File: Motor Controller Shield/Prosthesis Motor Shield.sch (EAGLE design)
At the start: 46 parts, among them M1_ACT M02POLAR_LOCK, M2_ACT M02POLAR_LOCK, U1 74VHC14MTCX, U2 74VHC14MTCX

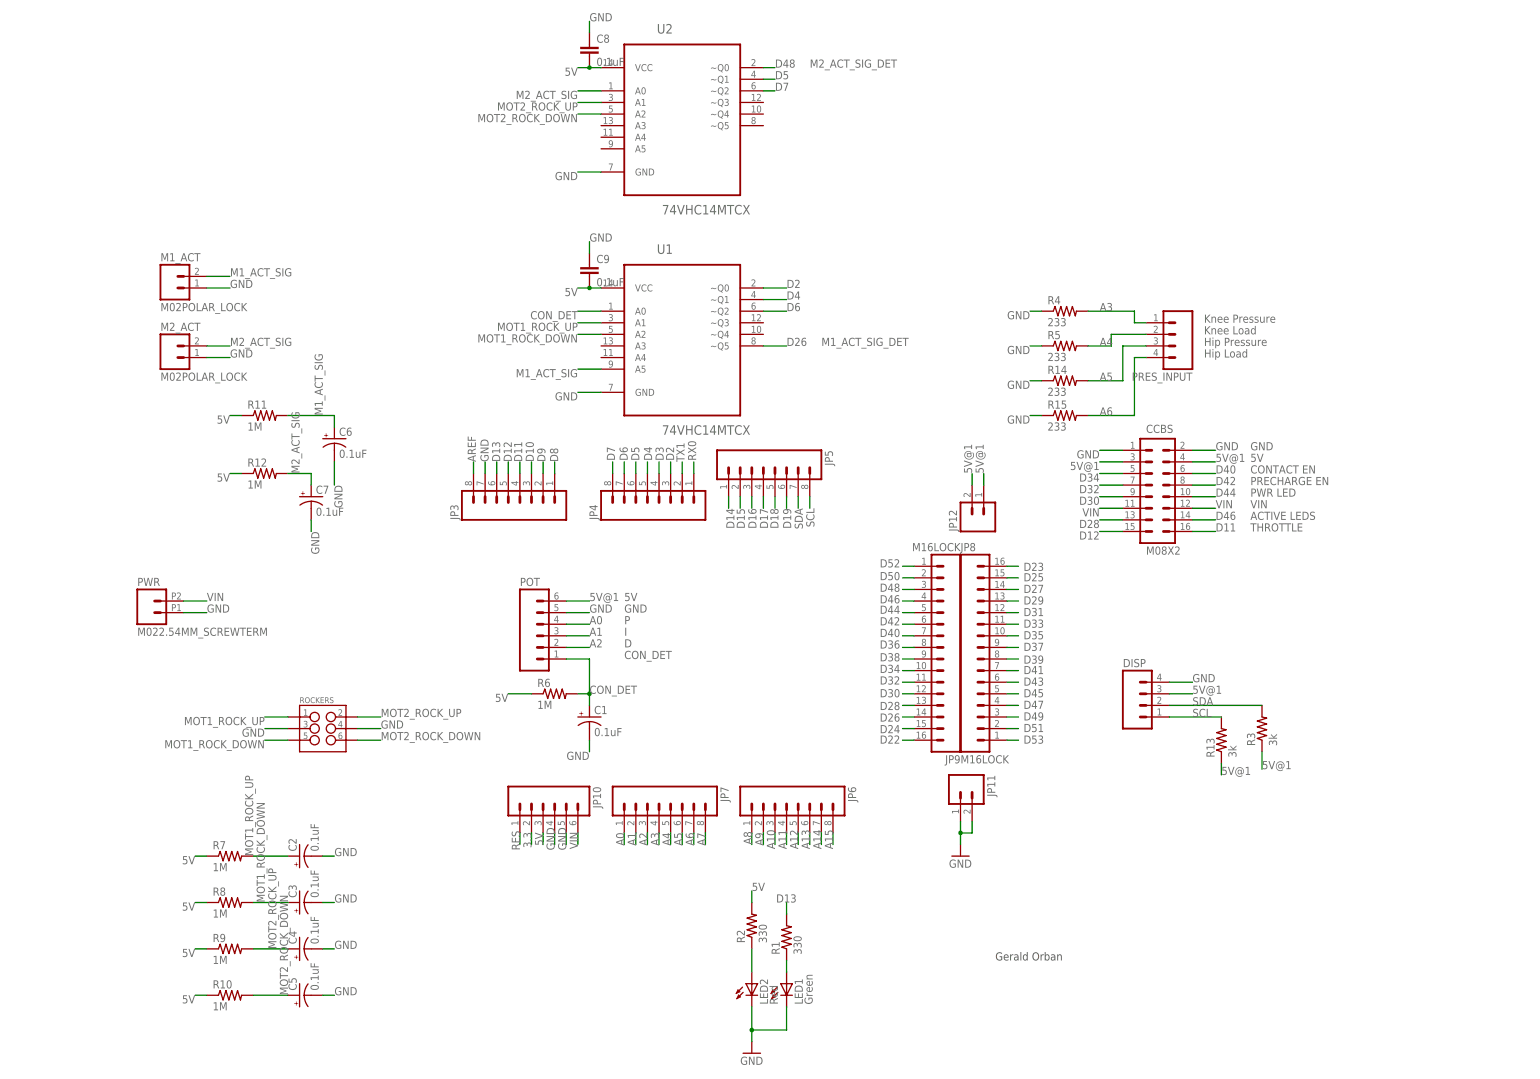
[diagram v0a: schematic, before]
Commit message: CHanged all connectors on MCB to use Molex
Changed most of the connectors on the BMS interface to use molex as
well.
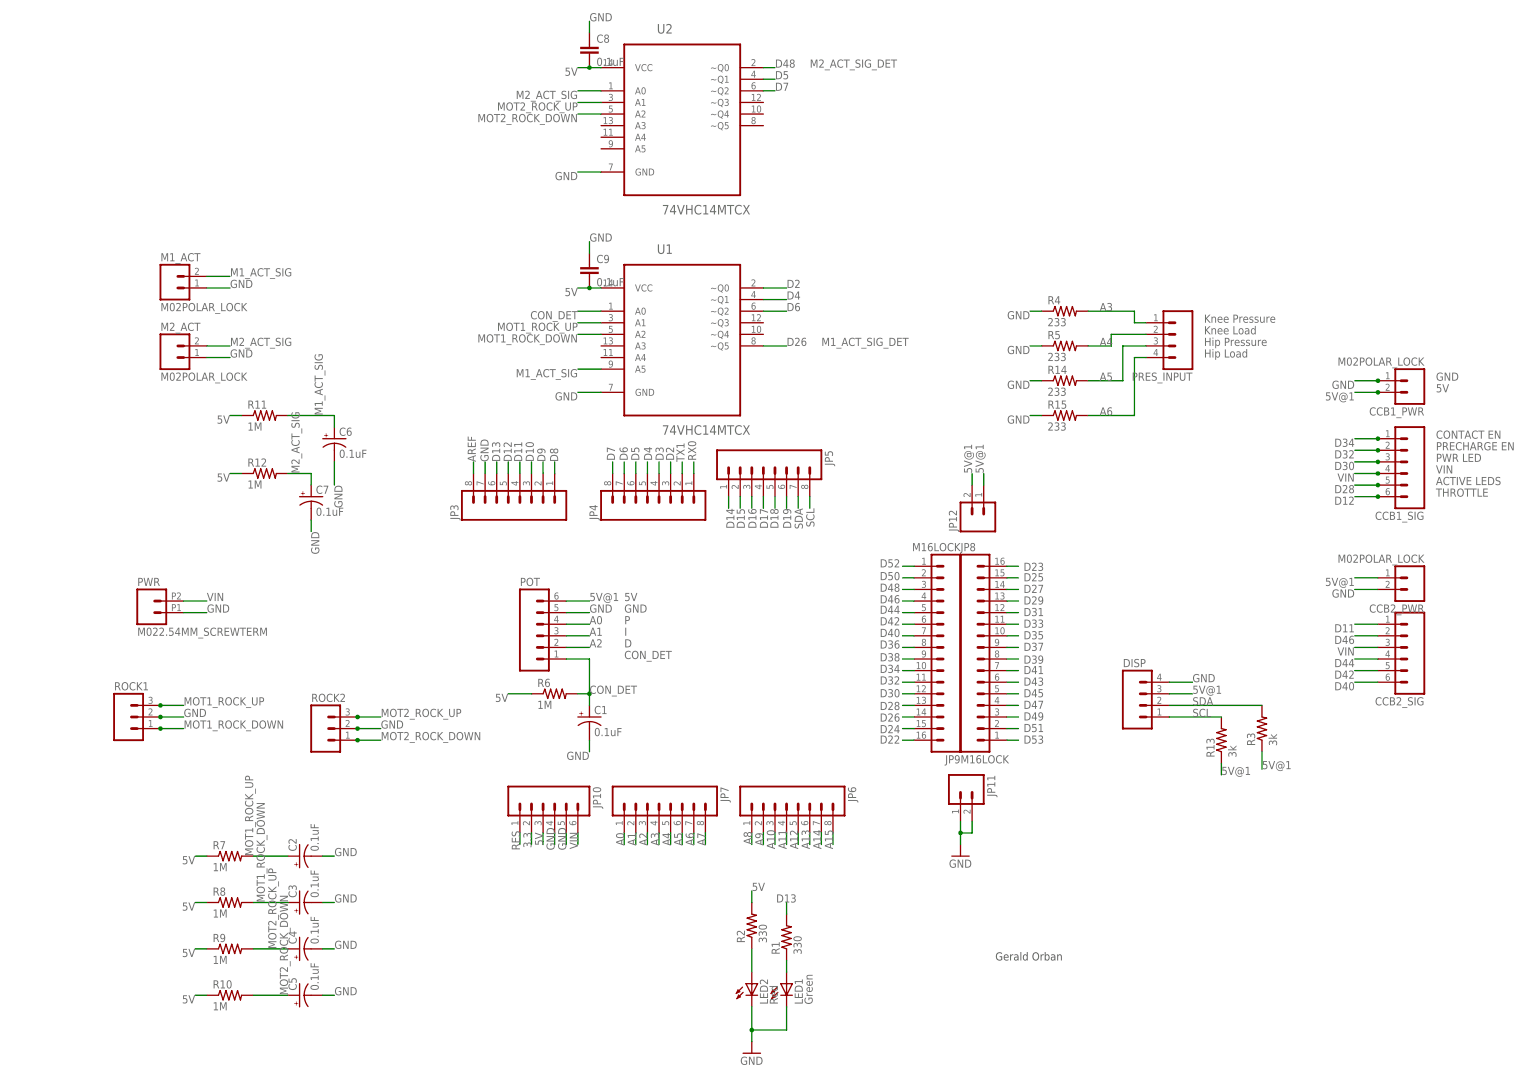
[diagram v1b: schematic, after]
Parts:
- removed CCBS: M08X2, SparkFun-Connectors:M08X2
- removed ROCKERS: (no value), SparkFun-Connectors:M03X2
- added CCB1_PWR, CCB2_PWR: M02POLAR_LOCK, SparkFun-Connectors:M02POLAR_LOCK
- added CCB1_SIG, CCB2_SIG: (no value), SparkFun-Connectors:M06POLAR_LOCK
- added ROCK1, ROCK2: (no value), SparkFun-Connectors:M03POLAR_LOCK
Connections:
- net 5V@1: now also CCB1_PWR.2, CCB2_PWR.1; no longer CCBS.3, CCBS.4
- net D11: now also CCB2_SIG.1; no longer CCBS.16
- net D12: now also CCB1_SIG.6; no longer CCBS.15
- net D28: now also CCB1_SIG.5; no longer CCBS.13
- net D30: now also CCB1_SIG.3; no longer CCBS.9
- net D32: now also CCB1_SIG.2; no longer CCBS.7
- net D34: now also CCB1_SIG.1; no longer CCBS.5
- net D40: now also CCB2_SIG.6; no longer CCBS.6
- net D42: now also CCB2_SIG.5; no longer CCBS.8
- net D44: now also CCB2_SIG.4; no longer CCBS.10
- net D46: now also CCB2_SIG.2; no longer CCBS.14
- net GND: now also CCB1_PWR.1, CCB2_PWR.2, ROCK1.2, ROCK2.2; no longer CCBS.1, CCBS.2, ROCKERS.3, ROCKERS.4
- net MOT1_ROCK_DOWN: now also ROCK1.1; no longer ROCKERS.5
- net MOT1_ROCK_UP: now also ROCK1.3; no longer ROCKERS.1
- net MOT2_ROCK_DOWN: now also ROCK2.1; no longer ROCKERS.6
- net MOT2_ROCK_UP: now also ROCK2.3; no longer ROCKERS.2
- net VIN: now also CCB1_SIG.4, CCB2_SIG.3; no longer CCBS.11, CCBS.12

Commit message: UPdating resistor packages to sizes which are
capable of disappating the appropriate amount of power.
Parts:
- R1, R2: device SparkFun-Passives:RESISTOR0603-RES -> SparkFun-Resistors:RESISTOR0805-RES
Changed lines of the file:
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@@
 <part name="GND2" library="SparkFun" deviceset="GND" device=""/>
 <part name="PWR" library="SparkFun-Connectors" deviceset="M02" device="2.54MM_SCREWTERM"/>
-<part name="R1" library="SparkFun-Passives" deviceset="RESISTOR" device="0603-RES" value="330"/>
-<part name="R2" library="SparkFun-Passives" deviceset="RESISTOR" device="0603-RES" value="330"/>
 <part name="LED1" library="SparkFun-LED" deviceset="LED" device="1206" value="Green"/>
 <part name="LED2" library="SparkFun-LED" deviceset="LED" device="1206" value="Red"/>
@@
 <part name="CCB1_PWR" library="SparkFun-Connectors" deviceset="M02" device="POLAR_LOCK"/>
 <part name="CCB2_PWR" library="SparkFun-Connectors" deviceset="M02" device="POLAR_LOCK"/>
+<part name="R2" library="SparkFun-Resistors" deviceset="RESISTOR" device="0805-RES" value="330"/>
+<part name="R1" library="SparkFun-Resistors" deviceset="RESISTOR" device="0805-RES" value="330"/>
 </parts>
 <sheets>
@@
 <instance part="GND2" gate="1" x="177.8" y="50.8"/>
 <instance part="PWR" gate="G$1" x="0" y="104.14"/>
-<instance part="R1" gate="G$1" x="139.7" y="33.02" rot="R90"/>
-<instance part="R2" gate="G$1" x="132.08" y="35.56" rot="R90"/>
 <instance part="LED1" gate="G$1" x="139.7" y="22.86"/>
 <instance part="LED2" gate="G$1" x="132.08" y="22.86"/>
@@
 <instance part="CCB1_PWR" gate="G$1" x="276.86" y="154.94" rot="R180"/>
 <instance part="CCB2_PWR" gate="G$1" x="276.86" y="111.76" rot="R180"/>
+<instance part="R2" gate="G$1" x="132.08" y="35.56" rot="R90"/>
+<instance part="R1" gate="G$1" x="139.7" y="33.02" rot="R90"/>
 </instances>
 <busses>
@@
 <segment>
 <wire x1="132.08" y1="30.48" x2="132.08" y2="25.4" width="0.1524" layer="91"/>
+<pinref part="LED2" gate="G$1" pin="A"/>
 <pinref part="R2" gate="G$1" pin="1"/>
-<pinref part="LED2" gate="G$1" pin="A"/>
 </segment>
 </net>
@@
 <segment>
 <wire x1="139.7" y1="27.94" x2="139.7" y2="25.4" width="0.1524" layer="91"/>
+<pinref part="LED1" gate="G$1" pin="A"/>
 <pinref part="R1" gate="G$1" pin="1"/>
-<pinref part="LED1" gate="G$1" pin="A"/>
-</segment>
-</net>
+</segment>
+</net>

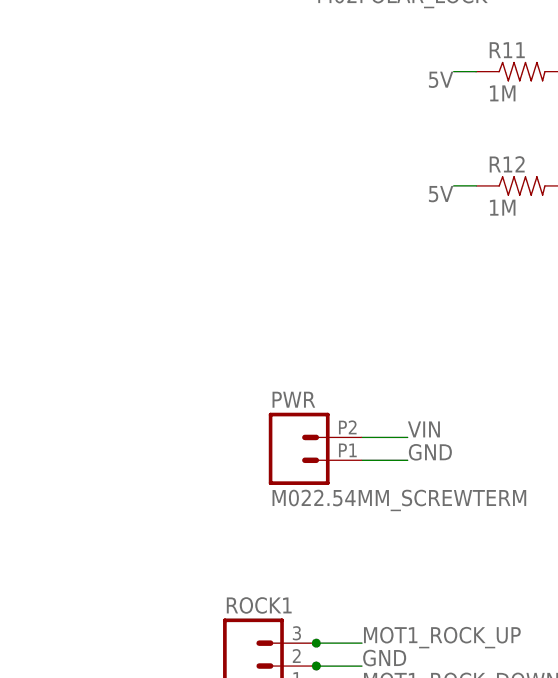
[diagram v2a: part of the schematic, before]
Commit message: Added capacitors for the three main boards
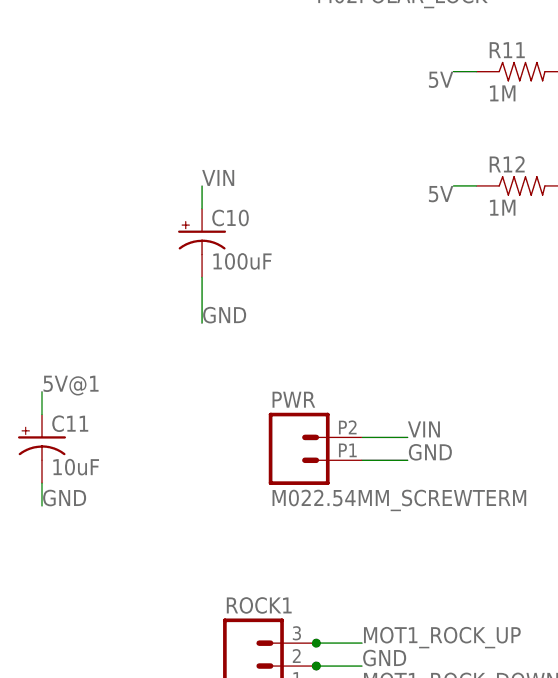
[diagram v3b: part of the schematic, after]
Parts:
- added C10: 100uF, SparkFun-Capacitors:CAP_POLPTH1
- added C11: 10uF, SparkFun-Capacitors:CAP_POLPTH2
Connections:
- net 5V@1: now also C11.+
- net GND: now also C10.-, C11.-
- net VIN: now also C10.+
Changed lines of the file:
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@@
 <part name="R2" library="SparkFun-Resistors" deviceset="RESISTOR" device="0805-RES" value="330"/>
 <part name="R1" library="SparkFun-Resistors" deviceset="RESISTOR" device="0805-RES" value="330"/>
+<part name="C10" library="SparkFun-Capacitors" deviceset="CAP_POL" device="PTH1" value="100uF"/>
+<part name="C11" library="SparkFun-Capacitors" deviceset="CAP_POL" device="PTH2" value="10uF"/>
 </parts>
 <sheets>
@@
 <instance part="R2" gate="G$1" x="132.08" y="35.56" rot="R90"/>
 <instance part="R1" gate="G$1" x="139.7" y="33.02" rot="R90"/>
+<instance part="C10" gate="G$1" x="-10.16" y="129.54"/>
+<instance part="C11" gate="G$1" x="-27.94" y="106.68"/>
 </instances>
 <busses>
@@
 <label x="96.52" y="185.42" size="1.778" layer="95"/>
 </segment>
+<segment>
+<pinref part="C10" gate="G$1" pin="-"/>
+<wire x1="-10.16" y1="124.46" x2="-10.16" y2="119.38" width="0.2032" layer="91"/>
+<label x="-10.16" y="119.38" size="1.778" layer="95"/>
+</segment>
+<segment>
+<wire x1="-27.94" y1="101.6" x2="-27.94" y2="99.06" width="0.2032" layer="91"/>
+<label x="-27.94" y="99.06" size="1.778" layer="95"/>
+<pinref part="C11" gate="G$1" pin="-"/>
+</segment>
 </net>
 <net name="VIN" class="0">
@@
 <label x="264.16" y="96.52" size="1.778" layer="95" rot="R180"/>
 <pinref part="CCB2_SIG" gate="G$1" pin="3"/>
+</segment>
+<segment>
+<pinref part="C10" gate="G$1" pin="+"/>
+<wire x1="-10.16" y1="132.08" x2="-10.16" y2="134.62" width="0.2032" layer="91"/>
+<label x="-10.16" y="134.62" size="1.778" layer="95"/>
 </segment>
 </net>
@@
 <pinref part="POT" gate="G$1" pin="6"/>
 </segment>
-</net>
+<segment>
+<wire x1="-27.94" y1="109.22" x2="-27.94" y2="111.76" width="0.2032" layer="91"/>
+<label x="-27.94" y="111.76" size="1.778" layer="95"/>
+<pinref part="C11" gate="G$1" pin="+"/>
+</segment>
+</net>
